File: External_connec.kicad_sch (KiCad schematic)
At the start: 12 parts, among them CN1 JST_Battery, J10 Conn_01x16_Socket, J2 A - B, J3 H - L, J4 TYPE-C-31-M12_13, J5 EXT_LOAD, J6 R4_TX, J7 R4_RX, J9 Conn_01x16_Socket

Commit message: Screw Terminal FPs
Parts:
- J2, J3: footprint (none) -> ESP32-S3_Dev_Board:3P_Screw_Terminal
- J5: footprint (none) -> ESP32-S3_Dev_Board:2P_Screw_Terminal
- J6, J7: footprint (none) -> ESP32-S3_Dev_Board:PinHeader_1x02_P2.54mm_Vertical
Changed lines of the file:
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@@
       (effects (font (size 1.27 1.27)) (justify left))
     )
-    (property "Footprint" "" (at 173.355 29.845 0)
+    (property "Footprint" "ESP32-S3_Dev_Board:2P_Screw_Terminal" (at 173.355 29.845 0)
       (effects (font (size 1.27 1.27)) hide)
     )
     (property "Datasheet" "~" (at 173.355 29.845 0)
+      (effects (font (size 1.27 1.27)) hide)
+    )
+    (property "PN" "" (at 173.355 29.845 0)
       (effects (font (size 1.27 1.27)) hide)
     )
@@
       (effects (font (size 1.27 1.27)) (justify left))
     )
-    (property "Footprint" "" (at 245.745 37.465 0)
+    (property "Footprint" "ESP32-S3_Dev_Board:PinHeader_1x02_P2.54mm_Vertical" (at 245.745 37.465 0)
       (effects (font (size 1.27 1.27)) hide)
     )
     (property "Datasheet" "~" (at 245.745 37.465 0)
+      (effects (font (size 1.27 1.27)) hide)
+    )
+    (property "PN" "" (at 245.745 37.465 0)
       (effects (font (size 1.27 1.27)) hide)
     )
@@
       (effects (font (size 1.27 1.27)) (justify left))
     )
-    (property "Footprint" "" (at 245.745 27.305 0)
+    (property "Footprint" "ESP32-S3_Dev_Board:PinHeader_1x02_P2.54mm_Vertical" (at 245.745 27.305 0)
       (effects (font (size 1.27 1.27)) hide)
     )
@@
       (effects (font (size 1.27 1.27)) hide)
     )
+    (property "PN" "" (at 245.745 27.305 0)
+      (effects (font (size 1.27 1.27)) hide)
+    )
     (pin "1")
     (pin "2")
@@
       (effects (font (size 1.27 1.27)) (justify left))
     )
-    (property "Footprint" "" (at 55.245 31.75 0)
+    (property "Footprint" "ESP32-S3_Dev_Board:3P_Screw_Terminal" (at 55.245 31.75 0)
       (effects (font (size 1.27 1.27)) hide)
     )
     (property "Datasheet" "~" (at 55.245 31.75 0)
+      (effects (font (size 1.27 1.27)) hide)
+    )
+    (property "PN" "" (at 55.245 31.75 0)
       (effects (font (size 1.27 1.27)) hide)
     )
@@
       (effects (font (size 1.27 1.27)) (justify left))
     )
-    (property "Footprint" "" (at 114.935 30.48 0)
+    (property "Footprint" "ESP32-S3_Dev_Board:3P_Screw_Terminal" (at 114.935 30.48 0)
       (effects (font (size 1.27 1.27)) hide)
     )
@@
       (effects (font (size 1.27 1.27)) hide)
     )
+    (property "PN" "" (at 114.935 30.48 0)
+      (effects (font (size 1.27 1.27)) hide)
+    )

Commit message: Instigated PCB Design
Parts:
- D11: PN (none) -> PRTR5V0U2X
- J10, J9: footprint (none) -> ESP32-S3_Dev_Board:PinHeader_2x08_P2.54mm_Vertical
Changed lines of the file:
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@@
       (effects (font (size 1.27 1.27)) (justify left top) hide)
+    )
+    (property "PN" "PRTR5V0U2X" (at 34.925 103.505 0)
+      (effects (font (size 1.27 1.27)) hide)
     )
     (pin "1")
@@
       (effects (font (size 1.27 1.27)) (justify left) hide)
     )
-    (property "Footprint" "" (at 200.025 86.995 0)
+    (property "Footprint" "ESP32-S3_Dev_Board:PinHeader_2x08_P2.54mm_Vertical" (at 200.025 86.995 0)
       (effects (font (size 1.27 1.27)) hide)
     )
@@
       (effects (font (size 1.27 1.27)) (justify left) hide)
     )
-    (property "Footprint" "" (at 170.815 86.995 0)
+    (property "Footprint" "ESP32-S3_Dev_Board:PinHeader_2x08_P2.54mm_Vertical" (at 170.815 86.995 0)
       (effects (font (size 1.27 1.27)) hide)
     )

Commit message: Changed USB C footprint and arranged components
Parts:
- J4: footprint ESP32-S3_Dev_Board:USB-C_SMD-TYPE-C-31-M-12 -> ESP32-S3_Dev_Board:tyye_c_connector
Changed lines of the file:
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@@
       (effects (font (size 1.27 1.27)))
     )
-    (property "Footprint" "ESP32-S3_Dev_Board:USB-C_SMD-TYPE-C-31-M-12" (at 63.5 94.615 90)
+    (property "Footprint" "ESP32-S3_Dev_Board:tyye_c_connector" (at 63.5 94.615 90)
       (effects (font (size 1.27 1.27)) hide)
     )

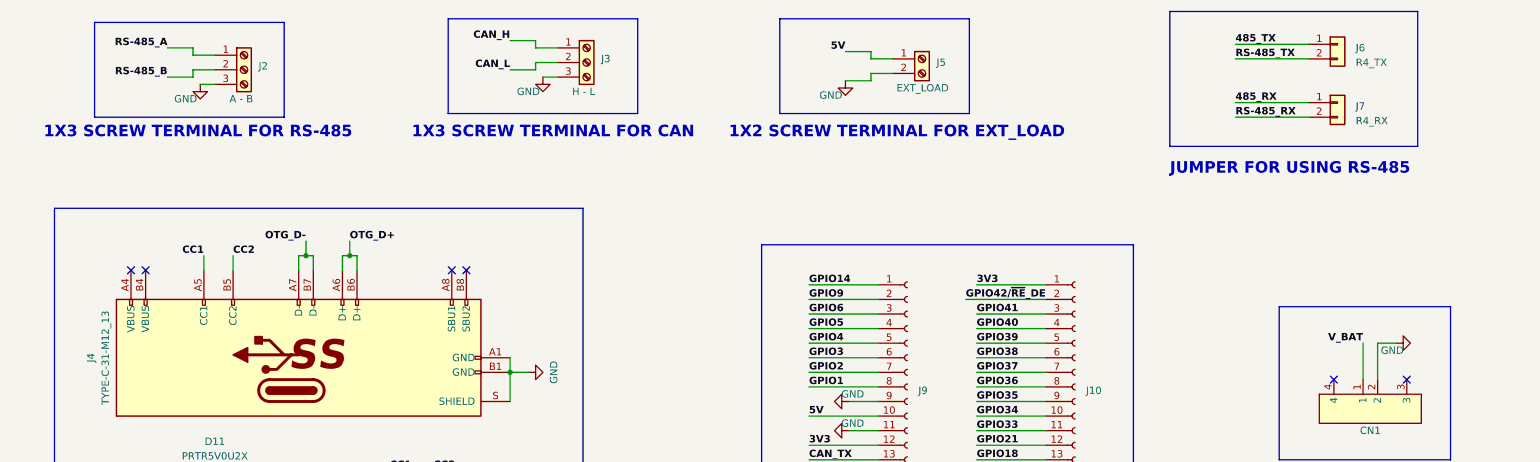
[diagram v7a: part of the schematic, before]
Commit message: Placed RS-485, CAN Transceiver and battery charger
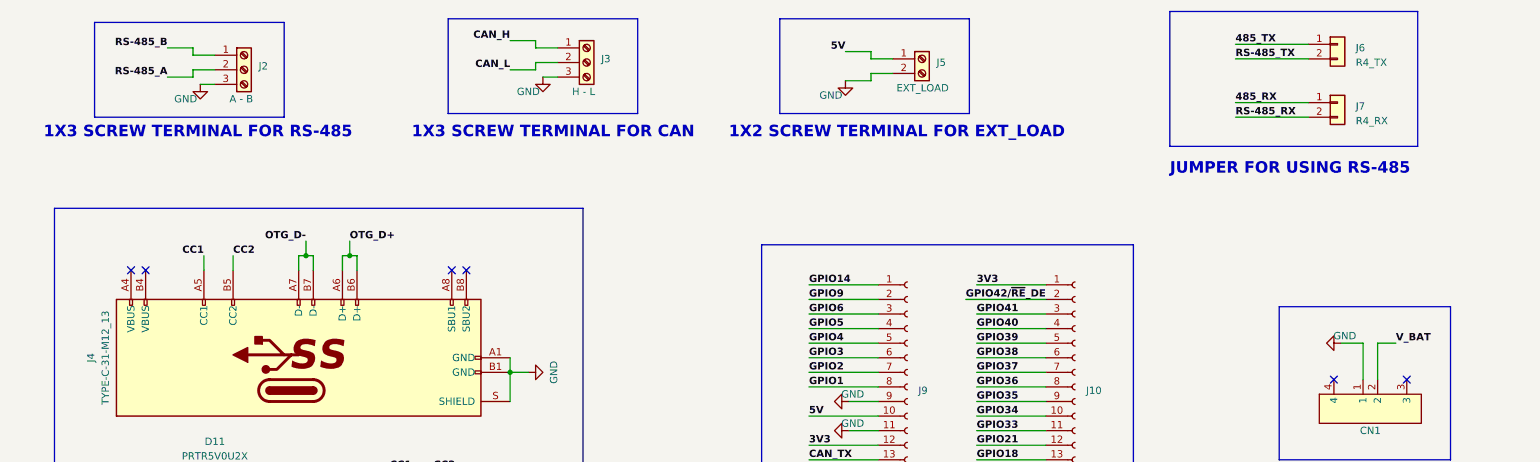
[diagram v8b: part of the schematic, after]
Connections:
- net GND: now also CN1.1; no longer CN1.2
- net RS-485_A: now also J2.2 (Pin_2); no longer J2.1 (Pin_1)
- net RS-485_B: now also J2.1 (Pin_1); no longer J2.2 (Pin_2)
- net V_BAT: now also CN1.2; no longer CN1.1
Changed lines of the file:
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@@
     (stroke (width 1) (type default) (color 72 72 72 1))
+  )
+  (wire (pts (xy 250.19 79.375) (xy 250.19 85.725))
+    (stroke (width 0) (type default))
   )
   (wire (pts (xy 74.93 64.135) (xy 74.93 66.675))
@@
     (stroke (width 0) (type default))
   )
+  (wire (pts (xy 246.38 79.375) (xy 250.19 79.375))
+    (stroke (width 0) (type default))
+  )
   (bus (pts (xy 62.23 23.495) (xy 62.23 40.005))
     (stroke (width 1) (type default) (color 72 72 72 1))
@@
   )
   (wire (pts (xy 125.73 172.085) (xy 116.205 172.085))
-    (stroke (width 0.5) (type default) (color 255 0 255 1))
+    (stroke (width 0.5) (type default) (color 132 132 0 1))
   )
   (wire (pts (xy 153.67 71.755) (xy 165.735 71.755))
@@
     (stroke (width 0) (type default))
   )
-  (wire (pts (xy 250.19 79.375) (xy 250.19 85.725))
-    (stroke (width 0) (type default))
-  )
   (wire (pts (xy 182.88 89.535) (xy 194.945 89.535))
     (stroke (width 0) (type default))
@@
     (effects (font (size 1.27 1.27) bold (color 0 0 255 1)) (justify right bottom))
   )
-  (label "V_BAT" (at 250.19 79.375 180) (fields_autoplaced)
-    (effects (font (size 1.27 1.27) bold (color 255 0 255 1)) (justify right bottom))
+  (label "V_BAT" (at 255.905 79.375 0) (fields_autoplaced)
+    (effects (font (size 1.27 1.27) bold (color 132 132 0 1)) (justify left bottom))
   )
   (label "GPIO34" (at 99.695 169.545 180) (fields_autoplaced)
@@
     (effects (font (size 1.27 1.27) bold (color 255 0 0 1)) (justify right bottom))
   )
-  (label "RS-485_A" (at 41.91 27.94 180) (fields_autoplaced)
+  (label "RS-485_A" (at 41.91 33.02 180) (fields_autoplaced)
     (effects (font (size 1.27 1.27) bold (color 0 0 0 1)) (justify right bottom))
   )
@@
     (effects (font (size 1.27 1.27) bold (color 72 0 0 1)) (justify right bottom))
   )
-  (label "RS-485_B" (at 41.91 33.02 180) (fields_autoplaced)
+  (label "RS-485_B" (at 41.91 27.94 180) (fields_autoplaced)
     (effects (font (size 1.27 1.27) bold (color 0 0 0 1)) (justify right bottom))
   )
   (label "V_BAT" (at 125.73 172.085 180) (fields_autoplaced)
-    (effects (font (size 1.27 1.27) bold (color 255 0 255 1)) (justify right bottom))
+    (effects (font (size 1.27 1.27) bold (color 132 132 0 1)) (justify right bottom))
   )
   (label "485_TX" (at 227.965 27.305 0) (fields_autoplaced)
@@
   )
   (hierarchical_label "V_BAT" (shape input) (at 116.205 172.085 180) (fields_autoplaced)
-    (effects (font (size 1.27 1.27) (thickness 0.254) bold (color 255 0 255 1)) (justify right))
+    (effects (font (size 1.27 1.27) (thickness 0.254) bold (color 132 132 0 1)) (justify right))
   )
   (hierarchical_label "RS-485_B" (shape input) (at 29.21 172.085 180) (fields_autoplaced)
@@
     )
   )
-  (symbol (lib_id "ESP32-S3_DB:GND") (at 255.905 79.375 90) (unit 1)
+  (symbol (lib_id "ESP32-S3_DB:GND") (at 246.38 79.375 270) (unit 1)
     (in_bom yes) (on_board yes) (dnp no)
-    (property "Reference" "#PWR062" (at 262.255 79.375 0)
-      (effects (font (size 1.27 1.27)) hide)
-    )
-    (property "Value" "GND" (at 255.27 80.645 90)
+    (property "Reference" "#PWR062" (at 240.03 79.375 0)
+      (effects (font (size 1.27 1.27)) hide)
+    )
+    (property "Value" "GND" (at 247.015 78.105 90)
       (effects (font (size 1.27 1.27)))
     )
-    (property "Footprint" "" (at 255.905 79.375 0)
-      (effects (font (size 1.27 1.27)) hide)
-    )
-    (property "Datasheet" "" (at 255.905 79.375 0)
-      (effects (font (size 1.27 1.27)) hide)
-    )
+    (property "Footprint" "" (at 246.38 79.375 0)
+      (effects (font (size 1.27 1.27)) hide)
+    )
+    (property "Datasheet" "" (at 246.38 79.375 0)
+      (effects (font (size 1.27 1.27)) hide)
+    )
